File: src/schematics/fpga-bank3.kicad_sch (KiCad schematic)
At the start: 7 parts, among them U6 LFE5U-85F-*BG756*

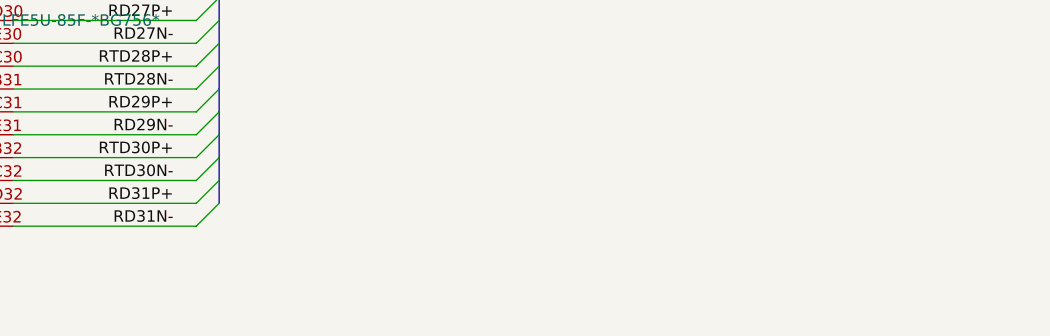
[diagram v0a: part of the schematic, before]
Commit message: Add notes on the schematic
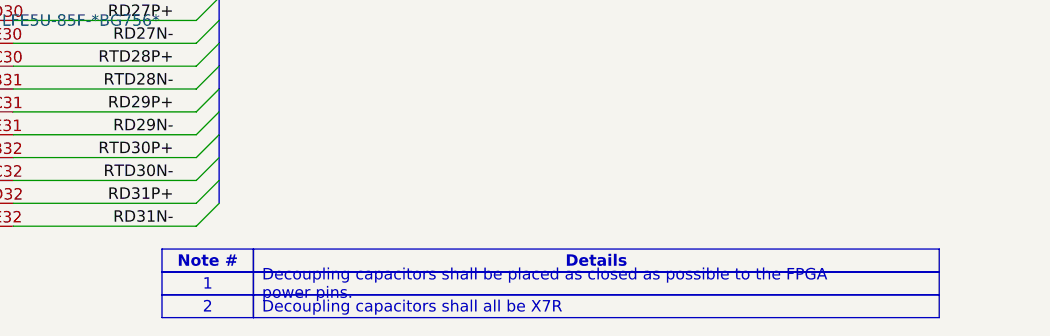
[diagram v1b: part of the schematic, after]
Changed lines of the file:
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@@
 		(comment 3 "${Part Number}")
+	)
+	(text_box "1"
+		(exclude_from_sim no)
+		(at 193.04 165.1 0)
+		(size 10.16 2.54)
+		(margins 0.9525 0.9525 0.9525 0.9525)
+		(stroke
+			(width 0)
+			(type solid)
+			(color 0 0 0 1)
+		)
+		(fill
+			(type none)
+		)
+		(effects
+			(font
+				(face "Arial")
+				(size 1.27 1.27)
+				(color 0 0 0 1)
+			)
+		)
+	)
+	(text_box "Decoupling capacitors shall all be X7R"
+		(exclude_from_sim no)
+		(at 203.2 167.64 0)
+		(size 76.2 2.54)
+		(margins 0.9525 0.9525 0.9525 0.9525)
+		(stroke
+			(width 0)
+			(type solid)
+			(color 0 0 0 1)
+		)
+		(fill
+			(type none)
+		)
+		(effects
+			(font
+				(face "Arial")
+				(size 1.27 1.27)
+				(color 0 0 0 1)
+			)
+			(justify left)
+		)
+	)
+	(text_box "Details"
+		(exclude_from_sim no)
+		(at 203.2 162.56 0)
+		(size 76.2 2.54)
+		(margins 0.9525 0.9525 0.9525 0.9525)
+		(stroke
+			(width 0)
+			(type solid)
+			(color 0 0 0 1)
+		)
+		(fill
+			(type none)
+		)
+		(effects
+			(font
+				(face "Arial")
+				(size 1.27 1.27)
+				(bold yes)
+				(color 0 0 0 1)
+			)
+		)
+	)
+	(text_box "2"
+		(exclude_from_sim no)
+		(at 193.04 167.64 0)
+		(size 10.16 2.54)
+		(margins 0.9525 0.9525 0.9525 0.9525)
+		(stroke
+			(width 0)
+			(type solid)
+			(color 0 0 0 1)
+		)
+		(fill
+			(type none)
+		)
+		(effects
+			(font
+				(face "Arial")
+				(size 1.27 1.27)
+				(color 0 0 0 1)
+			)
+		)
+	)
+	(text_box "Decoupling capacitors shall be placed as closed as possible to the FPGA power pins."
+		(exclude_from_sim no)
+		(at 203.2 165.1 0)
+		(size 76.2 2.54)
+		(margins 0.9525 0.9525 0.9525 0.9525)
+		(stroke
+			(width 0)
+			(type solid)
+			(color 0 0 0 1)
+		)
+		(fill
+			(type none)
+		)
+		(effects
+			(font
+				(face "Arial")
+				(size 1.27 1.27)
+				(color 0 0 0 1)
+			)
+			(justify left)
+		)
+	)
+	(text_box "Note #"
+		(exclude_from_sim no)
+		(at 193.04 162.56 0)
+		(size 10.16 2.54)
+		(margins 0.9525 0.9525 0.9525 0.9525)
+		(stroke
+			(width 0)
+			(type solid)
+			(color 0 0 0 1)
+		)
+		(fill
+			(type none)
+		)
+		(effects
+			(font
+				(face "Arial")
+				(size 1.27 1.27)
+				(bold yes)
+				(color 0 0 0 1)
+			)
+		)
 	)
 	(junction

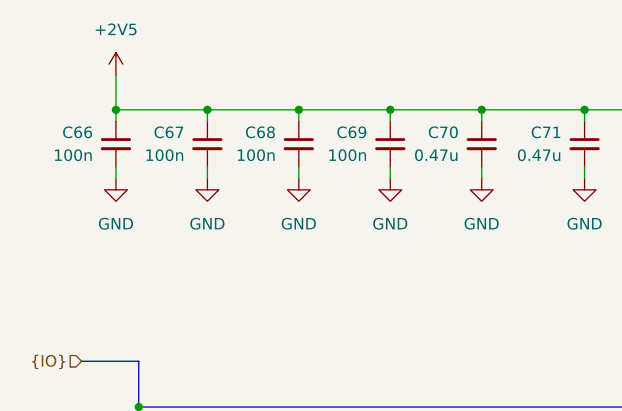
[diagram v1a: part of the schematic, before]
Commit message: Route the board power supply (#89)
* Replaces the inductors for smaller ones

* Starts routing the power supply

* Starts routing power

* Start adding power planes

* Adds decoupling capacitors

* Adds routing of the power sequencing

* Add routing for SRAM

* Route the SRAM data pins

* Finish routing the SRAM

* Route the SDRAM

* Move 1.8v converter to other side of the board

* Start routing DDR2 data lanes

* Use 0402 resistors instead of 0201 for emmc termination

* Route signals from DDR2 to FPGA bank

* Update routing of emmc

* Route the DDR2 without length matching

* Add length matching for DDR on L4 and L6. Todo L1 and redo L6

* Update routing of DDR2 L6 traces. Todo L1

* Finish routing of ddr2 traces

* Update power layer to support stripline for ddr2

* Fixed mechanical holes
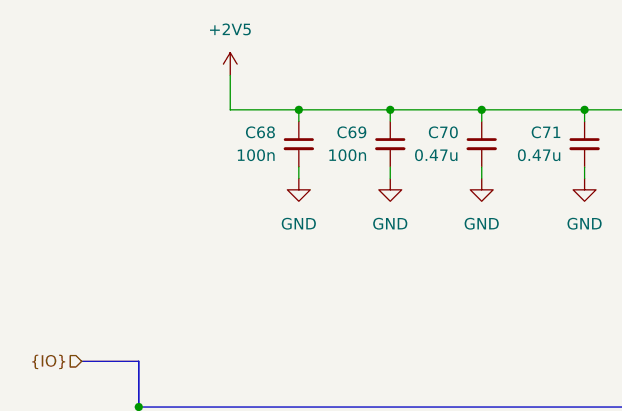
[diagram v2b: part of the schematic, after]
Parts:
- removed C66, C67: 100n, Capacitor_SMD:C_0402_1005Metric, symbol Device:C_Small
- C68, C69, C70, C71: footprint Capacitor_SMD:C_0402_1005Metric -> Capacitor_SMD:C_0201_0603Metric

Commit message: Start routing the connector
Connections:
- net RD25N- renamed RD25N
- net RD25P+ renamed RD25P
- net RD27N- renamed RD27N
- net RD27P+ renamed RD27P
- net RD29N- renamed RD29N
- net RD29P+ renamed RD29P
- net RD31N- renamed RD31N
- net RD31P+ renamed RD31P
- net RTD12N- renamed RTD12N
- net RTD12P+ renamed RTD12P
- net RTD13N- renamed RTD13N
- net RTD13P+ renamed RTD13P
- net RTD14N- renamed RTD14N
- net RTD14P+ renamed RTD14P
- net RTD15N- renamed RTD15N
- net RTD15P+ renamed RTD15P
- net RTD16N- renamed RTD16N
- net RTD16P+ renamed RTD16P
- net RTD17N- renamed RTD17N
- net RTD17P+ renamed RTD17P
- net RTD18N- renamed RTD18N
- net RTD18P+ renamed RTD18P
- net RTD19N- renamed RTD19N
- net RTD19P+ renamed RTD19P
- net RTD20N- renamed RTD20N
- net RTD20P+ renamed RTD20P
- net RTD21N- renamed RTD21N
- net RTD21P+ renamed RTD21P
- net RTD22N- renamed RTD22N
- net RTD22P+ renamed RTD22P
- net RTD23N- renamed RTD23N
- net RTD23P+ renamed RTD23P
- net RTD24N- renamed RTD24N
- net RTD24P+ renamed RTD24P
- net RTD26N- renamed RTD26N
- net RTD26P+ renamed RTD26P
- net RTD28N- renamed RTD28N
- net RTD28P+ renamed RTD28P
- net RTD30N- renamed RTD30N
- net RTD30P+ renamed RTD30P
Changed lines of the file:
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@@
 		)
 	)
-	(label "RTD12N-"
+	(label "RTD12N"
 		(at 120.65 78.74 0)
 		(effects
@@
 		)
 	)
-	(label "RTD13N-"
+	(label "RTD13N"
 		(at 120.65 88.9 0)
 		(effects
@@
 		)
 	)
-	(label "RTD19N-"
+	(label "RTD19N"
 		(at 120.65 149.86 0)
 		(effects
@@
 		)
 	)
-	(label "RTD24P+"
+	(label "RTD24P"
 		(at 194.31 121.92 180)
 		(effects
@@
 		)
 	)
-	(label "RTD18N-"
+	(label "RTD18N"
 		(at 120.65 139.7 0)
 		(effects
@@
 		)
 	)
-	(label "RTD21N-"
+	(label "RTD21N"
 		(at 194.31 93.98 180)
 		(effects
@@
 		)
 	)
-	(label "RTD18P+"
+	(label "RTD18P"
 		(at 120.65 137.16 0)
 		(effects
@@
 		)
 	)
-	(label "RD29P+"
+	(label "RD29P"
 		(at 194.31 147.32 180)
 		(effects
@@
 		)
 	)
-	(label "RTD20P+"
+	(label "RTD20P"
 		(at 120.65 157.48 0)
 		(effects
@@
 		)
 	)
-	(label "RTD21P+"
+	(label "RTD21P"
 		(at 194.31 91.44 180)
 		(effects
@@
 		)
 	)
-	(label "RD31P+"
+	(label "RD31P"
 		(at 194.31 157.48 180)
 		(effects
@@
 		)
 	)
-	(label "RTD22P+"
+	(label "RTD22P"
 		(at 194.0225 101.6 180)
 		(effects
@@
 		)
 	)
-	(label "RTD30P+"
+	(label "RTD30P"
 		(at 194.31 152.4 180)
 		(effects
@@
 		)
 	)
-	(label "RD31N-"
+	(label "RD31N"
 		(at 194.31 160.02 180)
 		(effects
@@
 		)
 	)
-	(label "RTD26P+"
+	(label "RTD26P"
 		(at 194.31 132.08 180)
 		(effects
@@
 		)
 	)
-	(label "RTD13P+"
+	(label "RTD13P"
 		(at 120.65 86.36 0)
 		(effects
@@
 		)
 	)
-	(label "RTD26N-"
+	(label "RTD26N"
 		(at 194.31 134.62 180)
 		(effects
@@
 		)
 	)
-	(label "RD25P+"
+	(label "RD25P"
 		(at 194.31 127 180)
 		(effects
@@
 		)
 	)
-	(label "RTD20N-"
+	(label "RTD20N"
 		(at 120.65 160.02 0)
 		(effects
@@
 		)
 	)
-	(label "RTD24N-"
+	(label "RTD24N"
 		(at 194.31 124.46 180)
 		(effects
@@
 		)
 	)
-	(label "RTD22N-"
+	(label "RTD22N"
 		(at 194.0225 104.14 180)
 		(effects
@@
 		)
 	)
-	(label "RTD23P+"
+	(label "RTD23P"
 		(at 194.31 111.76 180)
 		(effects
@@
 		)
 	)
-	(label "RTD30N-"
+	(label "RTD30N"
 		(at 194.31 154.94 180)
 		(effects
@@
 		)
 	)
-	(label "RTD12P+"
+	(label "RTD12P"
 		(at 120.65 76.2 0)
 		(effects
@@
 		)
 	)
-	(label "RTD28N-"
+	(label "RTD28N"
 		(at 194.31 144.78 180)
 		(effects
@@
 		)
 	)
-	(label "RTD16N-"
+	(label "RTD16N"
 		(at 120.65 119.38 0)
 		(effects
@@
 		)
 	)
-	(label "RTD14N-"
+	(label "RTD14N"
 		(at 120.65 99.06 0)
 		(effects
@@
 		)
 	)
-	(label "RTD17P+"
+	(label "RTD17P"
 		(at 120.65 127 0)
 		(effects
@@
 		)
 	)
-	(label "RTD17N-"
+	(label "RTD17N"
 		(at 120.65 129.54 0)
 		(effects
@@
 		)
 	)
-	(label "RTD16P+"
+	(label "RTD16P"
 		(at 120.65 116.84 0)
 		(effects
@@
 		)
 	)
-	(label "RD25N-"
+	(label "RD25N"
 		(at 194.31 129.54 180)
 		(effects
@@
 		)
 	)
-	(label "RTD28P+"
+	(label "RTD28P"
 		(at 194.31 142.24 180)
 		(effects
@@
 		)
 	)
-	(label "RD27N-"
+	(label "RD27N"
 		(at 194.31 139.7 180)
 		(effects
@@
 		)
 	)
-	(label "RTD19P+"
+	(label "RTD19P"
 		(at 120.65 147.32 0)
 		(effects
@@
 		)
 	)
-	(label "RTD15P+"
+	(label "RTD15P"
 		(at 120.65 106.68 0)
 		(effects
@@
 		)
 	)
-	(label "RD27P+"
+	(label "RD27P"
 		(at 194.31 137.16 180)
 		(effects
@@
 		)
 	)
-	(label "RTD15N-"
+	(label "RTD15N"
 		(at 120.65 109.22 0)
 		(effects
@@
 		)
 	)
-	(label "RTD23N-"
+	(label "RTD23N"
 		(at 194.31 114.3 180)
 		(effects
@@
 		)
 	)
-	(label "RTD14P+"
+	(label "RTD14P"
 		(at 120.65 96.52 0)
 		(effects
@@
 		)
 	)
-	(label "RD29N-"
+	(label "RD29N"
 		(at 194.31 149.86 180)
 		(effects

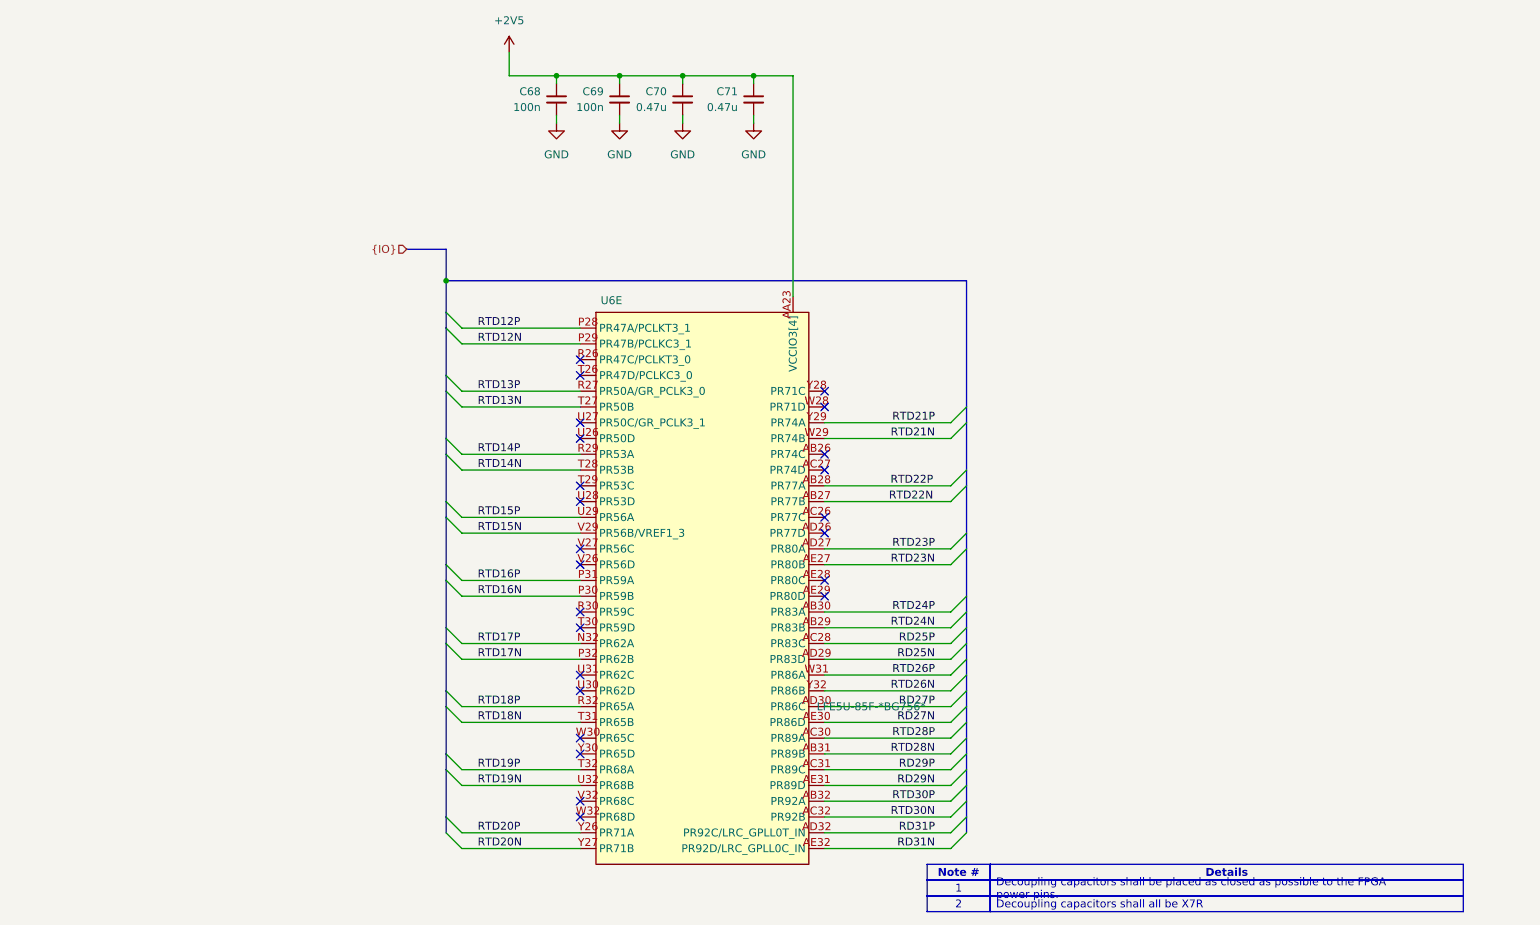
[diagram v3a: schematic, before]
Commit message: Continue routing the io connector
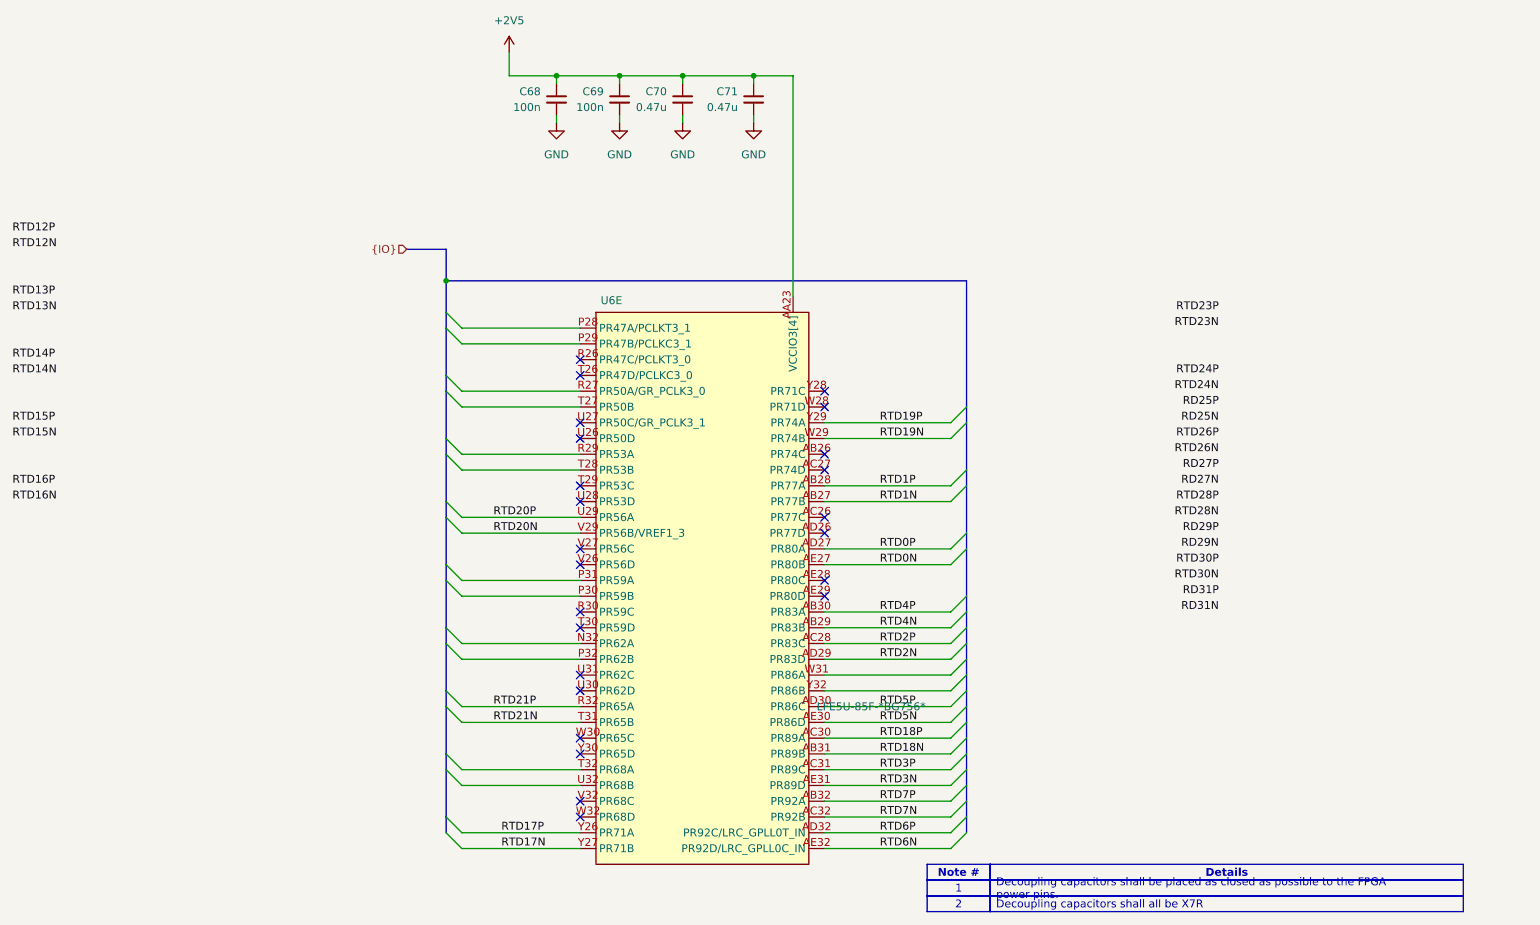
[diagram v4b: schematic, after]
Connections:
- net RD25N: no longer U6.AD29 (PR83D)
- net RD25P: no longer U6.AC28 (PR83C)
- net RD27N: no longer U6.AE30 (PR86D)
- net RD27P: no longer U6.AD30 (PR86C)
- net RD29N: no longer U6.AE31 (PR89D)
- net RD29P: no longer U6.AC31 (PR89C)
- net RD31N: no longer U6.AE32 (PR92D/LRC_GPLL0C_IN)
- net RD31P: no longer U6.AD32 (PR92C/LRC_GPLL0T_IN)
- net RTD12N: no longer U6.P29 (PR47B/PCLKC3_1)
- net RTD12P: no longer U6.P28 (PR47A/PCLKT3_1)
- net RTD13N: no longer U6.T27 (PR50B)
- net RTD13P: no longer U6.R27 (PR50A/GR_PCLK3_0)
- net RTD14N: no longer U6.T28 (PR53B)
- net RTD14P: no longer U6.R29 (PR53A)
- net RTD15N: no longer U6.V29 (PR56B/VREF1_3)
- net RTD15P: no longer U6.U29 (PR56A)
- net RTD16N: no longer U6.P30 (PR59B)
- net RTD16P: no longer U6.P31 (PR59A)
- net RTD17N: now also U6.Y27 (PR71B); no longer U6.P32 (PR62B)
- net RTD17P: now also U6.Y26 (PR71A); no longer U6.N32 (PR62A)
- net RTD18N: now also U6.AB31 (PR89B); no longer U6.T31 (PR65B)
- net RTD18P: now also U6.AC30 (PR89A); no longer U6.R32 (PR65A)
- net RTD19N: now also U6.W29 (PR74B); no longer U6.U32 (PR68B)
- net RTD19P: now also U6.Y29 (PR74A); no longer U6.T32 (PR68A)
- net RTD20N: now also U6.V29 (PR56B/VREF1_3); no longer U6.Y27 (PR71B)
- net RTD20P: now also U6.U29 (PR56A); no longer U6.Y26 (PR71A)
- net RTD21N: now also U6.T31 (PR65B); no longer U6.W29 (PR74B)
- net RTD21P: now also U6.R32 (PR65A); no longer U6.Y29 (PR74A)
- net RTD23N: no longer U6.AE27 (PR80B)
- net RTD23P: no longer U6.AD27 (PR80A)
- net RTD24N: no longer U6.AB29 (PR83B)
- net RTD24P: no longer U6.AB30 (PR83A)
- net RTD26N: no longer U6.Y32 (PR86B)
- net RTD26P: no longer U6.W31 (PR86A)
- net RTD28N: no longer U6.AB31 (PR89B)
- net RTD28P: no longer U6.AC30 (PR89A)
- net RTD30N: no longer U6.AC32 (PR92B)
- net RTD30P: no longer U6.AB32 (PR92A)
- net RTD22N renamed RTD1N
- net RTD22P renamed RTD1P
- new net RTD0N: U6.AE27 (PR80B)
- new net RTD0P: U6.AD27 (PR80A)
- new net RTD2N: U6.AD29 (PR83D)
- new net RTD2P: U6.AC28 (PR83C)
- new net RTD3N: U6.AE31 (PR89D)
- new net RTD3P: U6.AC31 (PR89C)
- new net RTD4N: U6.AB29 (PR83B)
- new net RTD4P: U6.AB30 (PR83A)
- new net RTD5N: U6.AE30 (PR86D)
- new net RTD5P: U6.AD30 (PR86C)
- new net RTD6N: U6.AE32 (PR92D/LRC_GPLL0C_IN)
- new net RTD6P: U6.AD32 (PR92C/LRC_GPLL0T_IN)
- new net RTD7N: U6.AC32 (PR92B)
- new net RTD7P: U6.AB32 (PR92A)
